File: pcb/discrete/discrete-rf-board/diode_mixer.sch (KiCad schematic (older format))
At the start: 30 parts, among them J30 UFL, J31 UFL, J32 UFL, J33 UFL, T5 HHM17147A1, T6 HHM17147A1, U22 BAT15-099R

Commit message: Autofill
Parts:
- R153, R154, R155, R156: footprint (none) -> Capacitor_SMD:C_0402_1005Metric; Mouser (none) -> 71-CRCW04020000Z0EDC
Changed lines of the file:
@@
 F 0 "R109" H 4430 3470 50  0000 L CNN
 F 1 "0R" H 4430 3410 50  0000 L CNN
-F 2 "" H 4400 3450 50  0001 C CNN
+F 2 "Capacitor_SMD:C_0402_1005Metric" H 4400 3450 50  0001 C CNN
 F 3 "~" H 4400 3450 50  0001 C CNN
+F 4 "71-CRCW04020000Z0EDC" H 4400 3450 50  0001 C CNN "Mouser"
 	1    4400 3450
 	0    -1   -1   0
@@
 F 0 "R110" H 4430 3770 50  0000 L CNN
 F 1 "0R" H 4430 3710 50  0000 L CNN
-F 2 "" H 4400 3750 50  0001 C CNN
+F 2 "Capacitor_SMD:C_0402_1005Metric" H 4400 3750 50  0001 C CNN
 F 3 "~" H 4400 3750 50  0001 C CNN
+F 4 "71-CRCW04020000Z0EDC" H 4400 3750 50  0001 C CNN "Mouser"
 	1    4400 3750
 	0    -1   -1   0
@@
 F 0 "R111" H 7530 3470 50  0000 L CNN
 F 1 "0R" H 7530 3410 50  0000 L CNN
-F 2 "" H 7500 3450 50  0001 C CNN
+F 2 "Capacitor_SMD:C_0402_1005Metric" H 7500 3450 50  0001 C CNN
 F 3 "~" H 7500 3450 50  0001 C CNN
+F 4 "71-CRCW04020000Z0EDC" H 7500 3450 50  0001 C CNN "Mouser"
 	1    7500 3450
 	0    -1   -1   0
@@
 F 0 "R112" H 7530 3770 50  0000 L CNN
 F 1 "0R" H 7530 3710 50  0000 L CNN
-F 2 "" H 7500 3750 50  0001 C CNN
+F 2 "Capacitor_SMD:C_0402_1005Metric" H 7500 3750 50  0001 C CNN
 F 3 "~" H 7500 3750 50  0001 C CNN
+F 4 "71-CRCW04020000Z0EDC" H 7500 3750 50  0001 C CNN "Mouser"
 	1    7500 3750
 	0    -1   -1   0

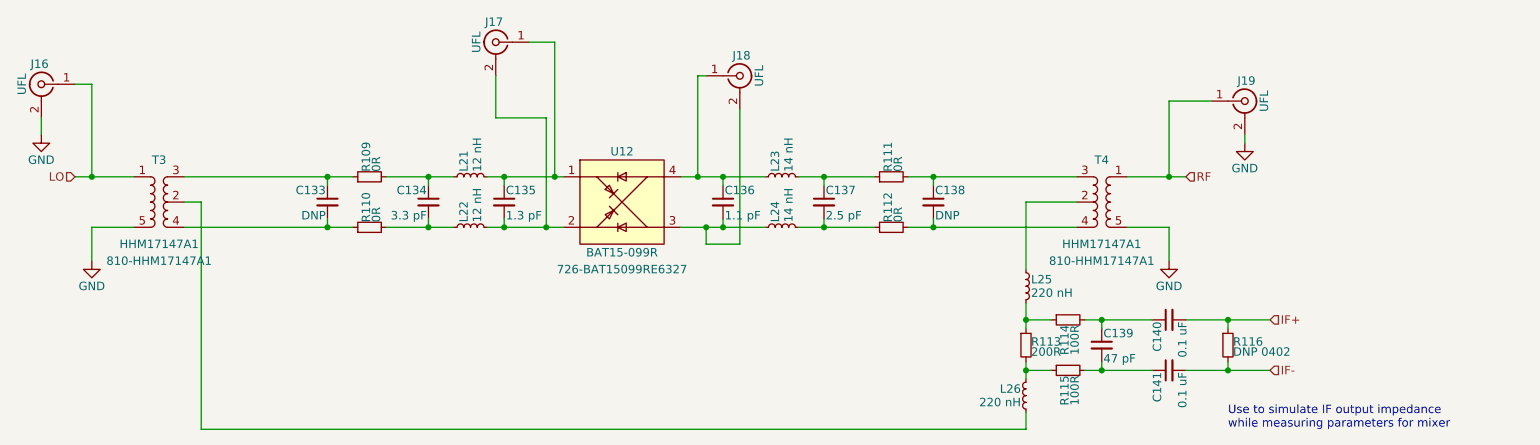
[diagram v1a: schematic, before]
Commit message: Add more footprints, saving before autofill
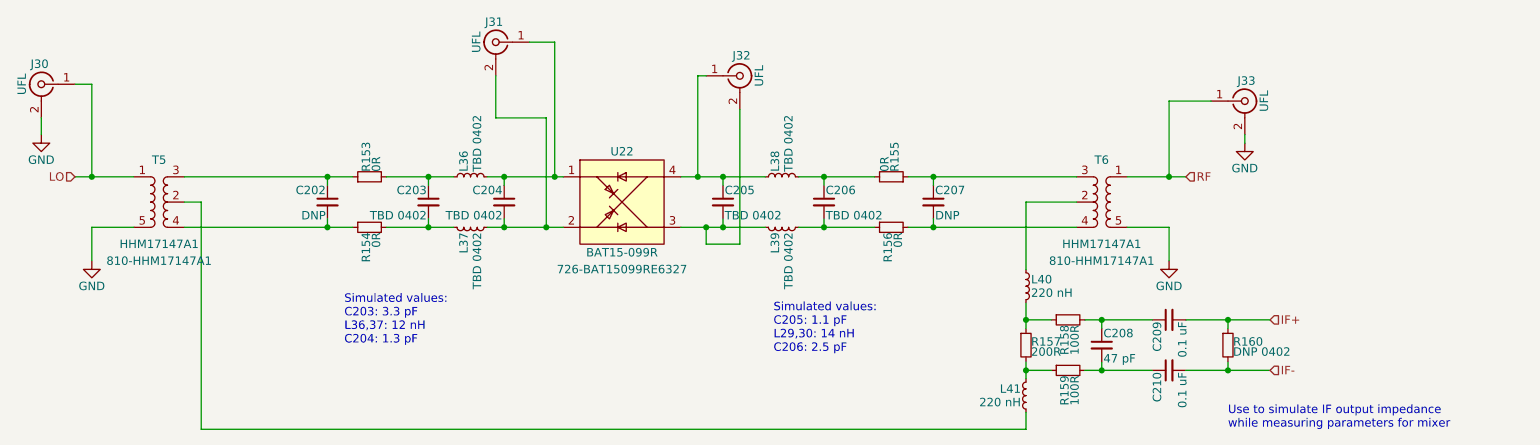
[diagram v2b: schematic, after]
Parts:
- C203: value 3.3 pF -> TBD 0402
- C204: value 1.3 pF -> TBD 0402
- C205: value 1.1 pF -> TBD 0402
- C206: value 2.5 pF -> TBD 0402
- L36, L37: value 12 nH -> TBD 0402
- L38, L39: value 14 nH -> TBD 0402
- R159: footprint (none) -> Resistor_SMD:R_0402_1005Metric; Mouser (none) -> 667-ERJ-U02D1000X
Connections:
- net at C206.1, L38.2: now also R155.2; no longer R155.1
- net at C207.1, T6.3 (+): now also R155.1; no longer R155.2
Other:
- note added: "Simulated values:\nC203: 3.3 pF\nL36,37: 12 nH\nC204: 1.3 pF"
- note added: "Simulated values:\nC205: 1.1 pF\nL29,30: 14 nH\nC206: 2.5 pF"
- moved on the sheet: L37, L39

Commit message: Autofill
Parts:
- C140, C141: footprint (none) -> Capacitor_SMD:C_0402_1005Metric; Mouser (none) -> 80-C0402C104M4P
- C203, C204, C206: footprint (none) -> Capacitor_SMD:C_0402_1005Metric; Mouser (none) -> 791-RF15N1R1B500CT
- R158: footprint (none) -> Resistor_SMD:R_0402_1005Metric; Mouser (none) -> 667-ERJ-U02D1000X
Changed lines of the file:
@@
 F 0 "C206" H 7110 3670 50  0000 L CNN
 F 1 "TBD 0402" H 7110 3520 50  0000 L CNN
-F 2 "" H 7100 3600 50  0001 C CNN
+F 2 "Capacitor_SMD:C_0402_1005Metric" H 7100 3600 50  0001 C CNN
 F 3 "~" H 7100 3600 50  0001 C CNN
+F 4 "791-RF15N1R1B500CT" H 7100 3600 50  0001 C CNN "Mouser"
 	1    7100 3600
 	1    0    0    -1
@@
 F 0 "R158" H 8580 4320 50  0000 L CNN
 F 1 "100R" H 8580 4260 50  0000 L CNN
-F 2 "" H 8550 4300 50  0001 C CNN
+F 2 "Resistor_SMD:R_0402_1005Metric" H 8550 4300 50  0001 C CNN
 F 3 "~" H 8550 4300 50  0001 C CNN
+F 4 " 667-ERJ-U02D1000X " H 8550 4300 50  0001 C CNN "Mouser"
 	1    8550 4300
 	0    -1   1    0
@@
 F 0 "C203" H 4760 3670 50  0000 L CNN
 F 1 "TBD 0402" H 4760 3520 50  0000 L CNN
-F 2 "" H 4750 3600 50  0001 C CNN
+F 2 "Capacitor_SMD:C_0402_1005Metric" H 4750 3600 50  0001 C CNN
 F 3 "~" H 4750 3600 50  0001 C CNN
+F 4 "791-RF15N1R1B500CT" H 4750 3600 50  0001 C CNN "Mouser"
 	1    4750 3600
 	-1   0    0    -1
@@
 F 0 "C209" H 9160 4370 50  0000 L CNN
 F 1 "0.1 uF" H 9160 4220 50  0000 L CNN
-F 2 "" H 9150 4300 50  0001 C CNN
+F 2 "Capacitor_SMD:C_0402_1005Metric" H 9150 4300 50  0001 C CNN
 F 3 "~" H 9150 4300 50  0001 C CNN
+F 4 "80-C0402C104M4P" H 9150 4300 50  0001 C CNN "Mouser"
 	1    9150 4300
 	0    -1   1    0
@@
 F 0 "C210" H 9160 4670 50  0000 L CNN
 F 1 "0.1 uF" H 9160 4520 50  0000 L CNN
-F 2 "" H 9150 4600 50  0001 C CNN
+F 2 "Capacitor_SMD:C_0402_1005Metric" H 9150 4600 50  0001 C CNN
 F 3 "~" H 9150 4600 50  0001 C CNN
+F 4 "80-C0402C104M4P" H 9150 4600 50  0001 C CNN "Mouser"
 	1    9150 4600
 	0    -1   1    0
@@
 F 0 "C204" H 5210 3670 50  0000 L CNN
 F 1 "TBD 0402" H 5210 3520 50  0000 L CNN
-F 2 "" H 5200 3600 50  0001 C CNN
+F 2 "Capacitor_SMD:C_0402_1005Metric" H 5200 3600 50  0001 C CNN
 F 3 "~" H 5200 3600 50  0001 C CNN
+F 4 "791-RF15N1R1B500CT" H 5200 3600 50  0001 C CNN "Mouser"
 	1    5200 3600
 	-1   0    0    -1

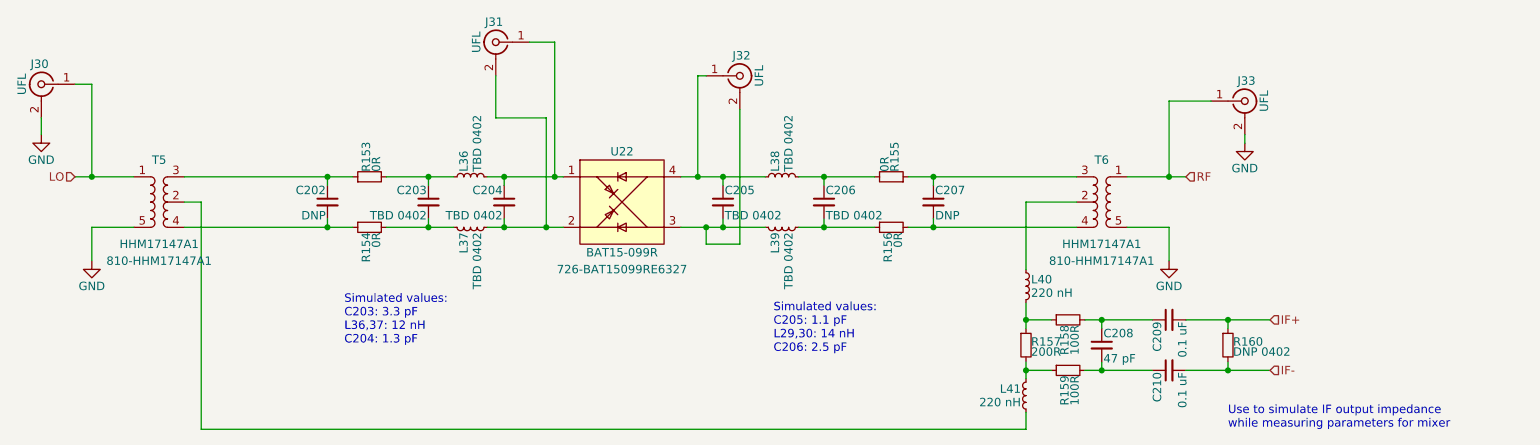
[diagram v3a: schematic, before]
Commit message: Reannotate everything; I'm trying to cut down the number of components
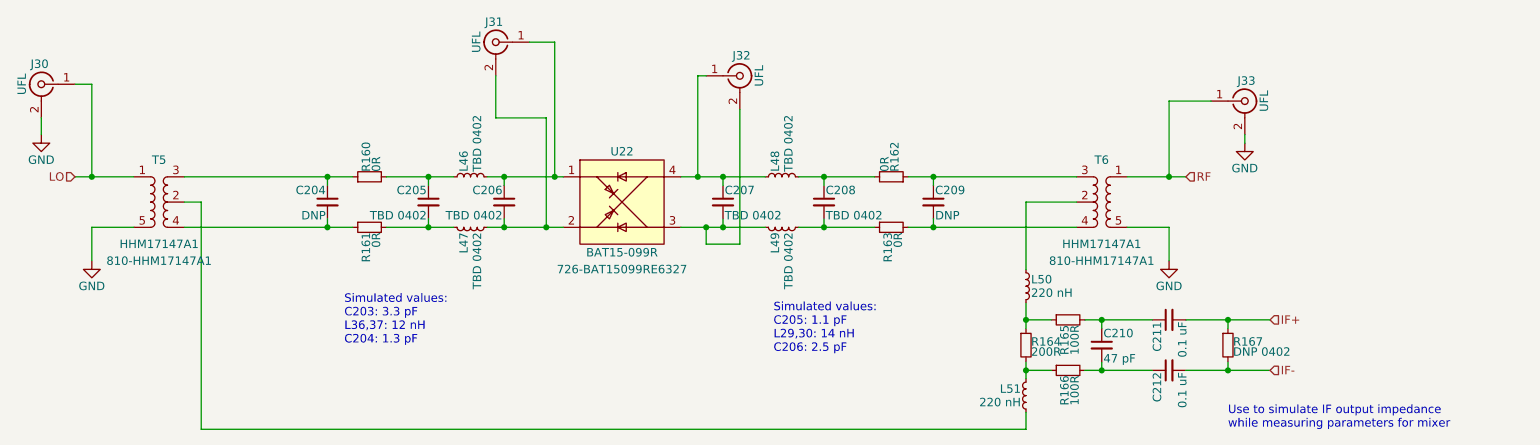
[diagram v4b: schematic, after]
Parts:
- renumbered C140 to C139, C141 to C140, C202 to C204, C203 to C205, C204 to C206, C205 to C207, C206 to C208, C207 to C209, C208 to C210, L36 to L46, L37 to L47, L38 to L48, L39 to L49, L40 to L50, L41 to L51, R153 to R160, R154 to R161, R155 to R162, R156 to R163, R157 to R164, R158 to R165, R159 to R166, R160 to R167

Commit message: Footprint a lot of stuff; save before autofill
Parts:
- R164: footprint (none) -> Resistor_SMD:R_0603_1608Metric_Pad1.05x0.95mm_HandSolder; Mouser (none) -> 71-CRCW0603200RFKEAC

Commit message: Autofill
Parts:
- L50, L51: footprint (none) -> Capacitor_SMD:C_0402_1005Metric; Mouser (none) -> 963-HK1005R22J-T
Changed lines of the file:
@@
 F 0 "L26" H 8330 4140 50  0000 L CNN
 F 1 "220 nH" H 8330 4060 50  0000 L CNN
-F 2 "" H 8300 4100 50  0001 C CNN
+F 2 "Capacitor_SMD:C_0402_1005Metric" H 8300 4100 50  0001 C CNN
 F 3 "~" H 8300 4100 50  0001 C CNN
+F 4 "963-HK1005R22J-T" H 8300 4100 50  0001 C CNN "Mouser"
 	1    8300 4100
 	1    0    0    -1
@@
 F 0 "L27" H 8330 4790 50  0000 L CNN
 F 1 "220 nH" H 8330 4710 50  0000 L CNN
-F 2 "" H 8300 4750 50  0001 C CNN
+F 2 "Capacitor_SMD:C_0402_1005Metric" H 8300 4750 50  0001 C CNN
 F 3 "~" H 8300 4750 50  0001 C CNN
+F 4 "963-HK1005R22J-T" H 8300 4750 50  0001 C CNN "Mouser"
 	1    8300 4750
 	-1   0    0    -1

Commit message: Add in a couple more components, save before autofill
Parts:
- C209: footprint (none) -> Capacitor_SMD:C_0402_1005Metric; Mouser (none) -> NoPart
- C210: footprint (none) -> Capacitor_SMD:C_0402_1005Metric; Mouser (none) -> 963-UMK105CG470JV-F

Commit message: Autofill
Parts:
- C204, L46, L47, L48, L49: footprint (none) -> Capacitor_SMD:C_0402_1005Metric; Mouser (none) -> NoPart
- R167: footprint (none) -> Resistor_SMD:R_0402_1005Metric; Mouser (none) -> NoPart
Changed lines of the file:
@@
 F 0 "L49" H 6880 3790 50  0000 L CNN
 F 1 "TBD 0402" H 6880 3710 50  0000 L CNN
-F 2 "" H 6850 3750 50  0001 C CNN
+F 2 "Capacitor_SMD:C_0402_1005Metric" H 6850 3750 50  0001 C CNN
 F 3 "~" H 6850 3750 50  0001 C CNN
+F 4 "NoPart" H 6850 3750 50  0001 C CNN "Mouser"
 	1    6850 3750
 	0    -1   1    0
@@
 F 0 "L48" H 6880 3490 50  0000 L CNN
 F 1 "TBD 0402" H 6880 3410 50  0000 L CNN
-F 2 "" H 6850 3450 50  0001 C CNN
+F 2 "Capacitor_SMD:C_0402_1005Metric" H 6850 3450 50  0001 C CNN
 F 3 "~" H 6850 3450 50  0001 C CNN
+F 4 "NoPart" H 6850 3450 50  0001 C CNN "Mouser"
 	1    6850 3450
 	0    -1   -1   0
@@
 F 0 "L47" H 5030 3790 50  0000 L CNN
 F 1 "TBD 0402" H 5030 3710 50  0000 L CNN
-F 2 "" H 5000 3750 50  0001 C CNN
+F 2 "Capacitor_SMD:C_0402_1005Metric" H 5000 3750 50  0001 C CNN
 F 3 "~" H 5000 3750 50  0001 C CNN
+F 4 "NoPart" H 5000 3750 50  0001 C CNN "Mouser"
 	1    5000 3750
 	0    -1   1    0
@@
 F 0 "C204" H 4160 3670 50  0000 L CNN
 F 1 "DNP" H 4160 3520 50  0000 L CNN
-F 2 "" H 4150 3600 50  0001 C CNN
+F 2 "Capacitor_SMD:C_0402_1005Metric" H 4150 3600 50  0001 C CNN
 F 3 "~" H 4150 3600 50  0001 C CNN
+F 4 "NoPart" H 4150 3600 50  0001 C CNN "Mouser"
 	1    4150 3600
 	-1   0    0    -1
@@
 F 0 "R167" H 9530 4470 50  0000 L CNN
 F 1 "DNP 0402" H 9530 4410 50  0000 L CNN
-F 2 "" H 9500 4450 50  0001 C CNN
+F 2 "Resistor_SMD:R_0402_1005Metric" H 9500 4450 50  0001 C CNN
 F 3 "~" H 9500 4450 50  0001 C CNN
+F 4 "NoPart" H 9500 4450 50  0001 C CNN "Mouser"
 	1    9500 4450
 	1    0    0    -1
@@
 F 0 "L46" H 5030 3490 50  0000 L CNN
 F 1 "TBD 0402" H 5030 3410 50  0000 L CNN
-F 2 "" H 5000 3450 50  0001 C CNN
+F 2 "Capacitor_SMD:C_0402_1005Metric" H 5000 3450 50  0001 C CNN
 F 3 "~" H 5000 3450 50  0001 C CNN
+F 4 "NoPart" H 5000 3450 50  0001 C CNN "Mouser"
 	1    5000 3450
 	0    -1   -1   0
